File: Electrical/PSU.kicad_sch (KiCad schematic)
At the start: 104 parts, among them IC2 SiC437AED-T1-GE3, J15 Conn_01x03_Pin, J16 USB_C_Receptacle_USB2.0, Q10 2N7002, Q8 2N7002, Q9 2N7002, SW1 SW_Push, U12 ADP1715ARMZ-R7, U13 HT7533, U14 CH224Q_C46061833, U15 SY8253ADC, U16 SY8253ADC, U6 SY8253ADC

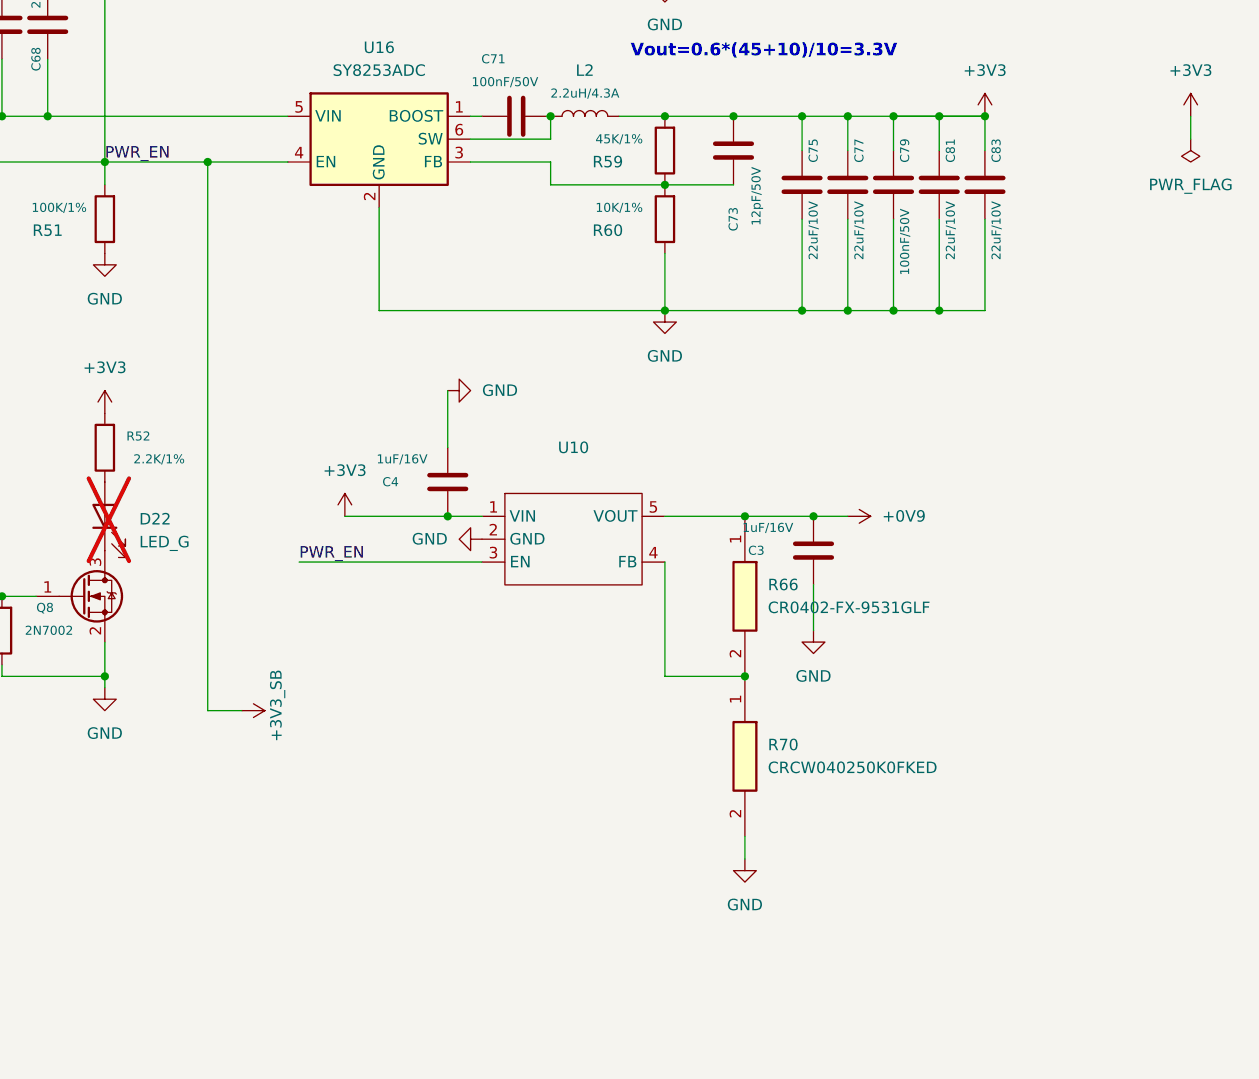
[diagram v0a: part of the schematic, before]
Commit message: update 0.9v regulator
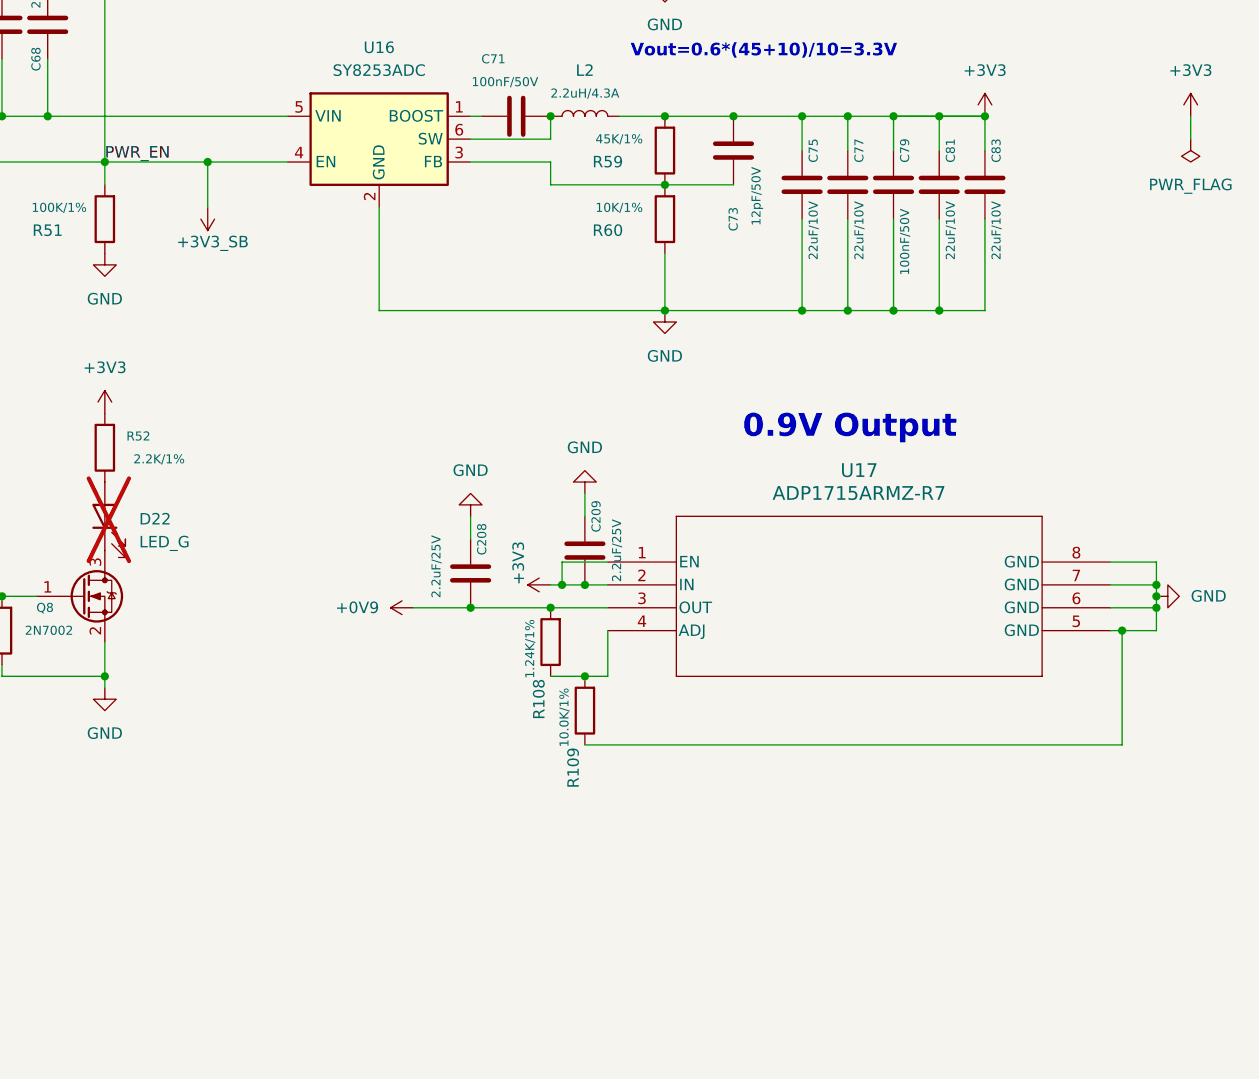
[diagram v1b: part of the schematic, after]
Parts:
- removed C3, C4: 1uF/16V, A_HDJ_Library:C_0402_1005Metric, symbol Device:C
- removed R66: CR0402-FX-9531GLF, RESC1005X40N, symbol 9.53k resis:CR0402-FX-9531GLF
- removed R70: CRCW040250K0FKED, RESC1005X40N, symbol 50k resis:CRCW040250K0FKED
- removed U10: (no value), Package_TO_SOT_SMD:SOT-23-5, symbol ldo:BL8079AGCB5TR
- added C208, C209: 2.2uF/25V, Capacitor_SMD:C_0603_1608Metric_Pad1.08x0.95mm_HandSolder, symbol Device:C
- added R108: 1.24K/1%, Resistor_SMD:R_0201_0603Metric_Pad0.64x0.40mm_HandSolder, symbol Device:R
- added R109: 10.0K/1%, Resistor_SMD:R_0201_0603Metric_Pad0.64x0.40mm_HandSolder, symbol Device:R
- added U17: ADP1715ARMZ-R7, 1v ldo:RM_8_ADI, symbol 1v ldo:ADP1715ARMZ-R7
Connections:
- net +0V9: now also C208.1, R108.2, U17.3 (OUT)
- net +3V3: now also C209.1, U17.1 (EN), U17.2 (IN)
- net GND: now also C208.2, C209.2, R109.1, U17.5 (GND), U17.6 (GND), U17.7 (GND), U17.8 (GND)
- new net: R108.1, R109.2, U17.4 (ADJ)
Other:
- note added: "0.9V Output"

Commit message: Revert "update 0.9v regulator"
This reverts commit 20026994f1eba6e61bd33e858c390714c2ea728b.
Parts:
- removed C208, C209: 2.2uF/25V, Capacitor_SMD:C_0603_1608Metric_Pad1.08x0.95mm_HandSolder, symbol Device:C
- removed R108: 1.24K/1%, Resistor_SMD:R_0201_0603Metric_Pad0.64x0.40mm_HandSolder, symbol Device:R
- removed R109: 10.0K/1%, Resistor_SMD:R_0201_0603Metric_Pad0.64x0.40mm_HandSolder, symbol Device:R
- removed U17: ADP1715ARMZ-R7, 1v ldo:RM_8_ADI, symbol 1v ldo:ADP1715ARMZ-R7
- added C3, C4: 1uF/16V, A_HDJ_Library:C_0402_1005Metric, symbol Device:C
- added R66: CR0402-FX-9531GLF, RESC1005X40N, symbol 9.53k resis:CR0402-FX-9531GLF
- added R70: CRCW040250K0FKED, RESC1005X40N, symbol 50k resis:CRCW040250K0FKED
- added U10: (no value), Package_TO_SOT_SMD:SOT-23-5, symbol ldo:BL8079AGCB5TR
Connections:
- net +0V9: now also C3.1, R66.1, U10.5 (VOUT)
- net +3V3: now also C4.2, U10.1 (VIN)
- net +3V3_SB: now also U10.3 (EN)
- net GND: now also C3.2, C4.1, R70.2, U10.2 (GND)
- new net: R66.2, R70.1, U10.4 (FB)
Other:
- note removed: "0.9V Output"
